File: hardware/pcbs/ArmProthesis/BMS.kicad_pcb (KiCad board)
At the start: 4 copper layers, 96.9 x 57 mm, 59 parts, among them J1 XT60-M, J2 XT60-F, J3 4-1971800-1, Q1 BSC014N04LSIATMA1, Q2 BSC014N04LSIATMA1, Q3 BSS84, SW1 CK_KMS2xxG, SW2 CK_KMS2xxG, SW3 CK_KMS2xxG, U1 BQ76920PW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

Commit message: sEMG critical  issue
Corrected inaccurate DIN 1.5mm jack footprint
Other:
- board text added: "BMS v0.3"
- board text removed: "BMS v0.2"
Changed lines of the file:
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@@
 		(layer "Edge.Cuts")
 	)
-	(gr_text "BMS v0.2"
+	(gr_text "BMS v0.3"
 		(at 189.6 126.5 0)
 		(layer "B.SilkS")

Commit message: .
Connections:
- R5 pad 1: Net-(U1-VC2) -> Net-(U1-VC5)
- U1 pad 12: Net-(U1-VC2) -> Net-(U1-VC5)
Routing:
- net Net-(U1-VC5): track 0.00 -> 4.03 mm
- net Net-(U1-VC2): track 7.32 -> 3.37 mm
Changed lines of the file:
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@@
 	(net 45 "Net-(Q1-S)")
 	(net 46 "/BMS_GND")
+	(net 47 "Net-(U1-VC5)")
 	(footprint "Capacitor_SMD:C_0603_1608Metric_Pad1.08x0.95mm_HandSolder"
 		(layer "F.Cu")
@@
 			(layers "F.Cu" "F.Mask" "F.Paste")
 			(roundrect_rratio 0.25)
-			(net 13 "Net-(U1-VC2)")
+			(net 47 "Net-(U1-VC5)")
 			(pinfunction "VC5")
 			(pintype "input")
@@
 			(layers "F.Cu" "F.Mask" "F.Paste")
 			(roundrect_rratio 0.25)
-			(net 13 "Net-(U1-VC2)")
+			(net 47 "Net-(U1-VC5)")
 			(pintype "passive")
 		)
@@
 	(gr_rect
 		(start 154.0545 94.25)
-		(end 155.4545 96.385)
+		(end 155.4545 95.738247)
 		(stroke
 			(width 0.2)
@@
 	)
 	(segment
-		(start 157.62 97.495)
-		(end 156.42 96.295)
-		(width 0.3)
-		(layer "F.Cu")
-		(net 13)
-	)
-	(segment
-		(start 154.802 95.59)
-		(end 154.747 95.645)
+		(start 156.422775 94.997775)
+		(end 156.9475 95.5225)
 		(width 0.3)
 		(layer "F.Cu")
@@
 	)
 	(segment
-		(start 157.902 95.525)
+		(start 156.9475 95.5225)
 		(end 157.9045 95.5225)
 		(width 0.3)
@@
 	)
 	(segment
-		(start 156.42 96.295)
-		(end 154.747 96.295)
-		(width 0.3)
-		(layer "F.Cu")
-		(net 13)
-	)
-	(segment
-		(start 158.28 97.495)
-		(end 157.62 97.495)
-		(width 0.3)
-		(layer "F.Cu")
-		(net 13)
-	)
-	(segment
-		(start 154.867 95.525)
-		(end 157.902 95.525)
-		(width 0.3)
-		(layer "F.Cu")
-		(net 13)
-	)
-	(segment
-		(start 154.747 95.645)
-		(end 154.867 95.525)
+		(start 154.7545 94.997775)
+		(end 156.422775 94.997775)
 		(width 0.3)
 		(layer "F.Cu")
@@
 		(net 46)
 	)
+	(segment
+		(start 157.62 97.495)
+		(end 156.42 96.295)
+		(width 0.3)
+		(layer "F.Cu")
+		(net 47)
+	)
+	(segment
+		(start 156.42 96.295)
+		(end 154.747 96.295)
+		(width 0.3)
+		(layer "F.Cu")
+		(net 47)
+	)
+	(segment
+		(start 158.28 97.495)
+		(end 157.62 97.495)
+		(width 0.3)
+		(layer "F.Cu")
+		(net 47)
+	)
 	(zone

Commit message: Corrected BMS connection
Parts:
- moved R13 0.43 mm to (130.1, 97.2)
- moved U2 0.43 mm to (129.2, 94.0)
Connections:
- R13 pad 2: Net-(U1-VC1) -> PACK+
- SW1 pad 1: Net-(U1-VC1) -> PACK+
- U2 pad 1: Net-(U1-VC1) -> PACK+
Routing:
- net Net-(U1-VC1): track 39.2 -> 3.54 mm, vias 2 -> 0
- net PACK+: track 121.0 -> 146.0 mm
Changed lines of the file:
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@@
 	(footprint "Resistor_SMD:R_0603_1608Metric_Pad0.98x0.95mm_HandSolder"
 		(layer "F.Cu")
-		(at 130.525 97.25)
+		(at 130.1 97.25)
 		(descr "Resistor SMD 0603 (1608 Metric), square (rectangular) end terminal, IPC_7351 nominal with elongated pad for handsoldering. (Body size source: IPC-SM-782 page 72, https://www.pcb-3d.com/wordpress/wp-content/uploads/ipc-sm-782a_amendment_1_and_2.pdf), generated with kicad-footprint-generator")
 		(tags "resistor handsolder")
@@
 			(layers "F.Cu" "F.Mask" "F.Paste")
 			(roundrect_rratio 0.25)
-			(net 11 "Net-(U1-VC1)")
+			(net 26 "PACK+")
 			(pintype "passive")
 		)
@@
 	(footprint "Package_TO_SOT_SMD:SOT-23-6_Handsoldering"
 		(layer "F.Cu")
-		(at 129.65 93.95 180)
+		(at 129.225 93.95 180)
 		(descr "6-pin SOT-23 package, Handsoldering")
 		(tags "SOT-23-6 Handsoldering")
@@
 			(layers "F.Cu" "F.Mask" "F.Paste")
 			(roundrect_rratio 0.25)
-			(net 11 "Net-(U1-VC1)")
+			(net 26 "PACK+")
 			(pinfunction "VCCA")
 			(pintype "power_in")
@@
 			(layers "F.Cu" "F.Mask" "F.Paste")
 			(roundrect_rratio 0.15)
-			(net 11 "Net-(U1-VC1)")
+			(net 26 "PACK+")
 			(pinfunction "1")
 			(pintype "passive")
@@
 			(layers "F.Cu" "F.Mask" "F.Paste")
 			(roundrect_rratio 0.15)
-			(net 11 "Net-(U1-VC1)")
+			(net 26 "PACK+")
 			(pinfunction "1")
 			(pintype "passive")
@@
 	)
 	(segment
-		(start 128.3 94.9)
-		(end 126.75 94.9)
+		(start 127.875 94.9)
+		(end 126.325 94.9)
 		(width 0.5)
 		(layer "F.Cu")
@@
 	)
 	(via
-		(at 126.75 94.9)
+		(at 126.325 94.9)
 		(size 0.8)
 		(drill 0.4)
@@
 	)
 	(segment
-		(start 134.5 95.2)
-		(end 133.5158 95.2)
-		(width 0.5)
-		(layer "F.Cu")
-		(net 7)
-	)
-	(segment
 		(start 162.987 92.47)
 		(end 162.977 92.48)
@@
 	)
 	(segment
+		(start 134.5 95.2)
+		(end 133.5158 95.2)
+		(width 0.5)
+		(layer "F.Cu")
+		(net 7)
+	)
+	(segment
 		(start 147.855 92.395)
 		(end 149.022 92.395)
@@
 	)
 	(segment
-		(start 131 93.95)
-		(end 132.575 93.95)
-		(width 0.5)
-		(layer "F.Cu")
-		(net 7)
-	)
-	(segment
 		(start 141.1 95.55)
 		(end 141.1045 95.5455)
@@
 	)
 	(segment
+		(start 130.7125 93.95)
+		(end 132.05 93.95)
+		(width 0.5)
+		(layer "F.Cu")
+		(net 7)
+	)
+	(segment
 		(start 151.4125 88.1)
 		(end 151.4125 89.1)
@@
 	)
 	(via
-		(at 132.575 93.95)
+		(at 132.05 93.95)
 		(size 0.8)
 		(drill 0.4)
@@
 	)
 	(segment
-		(start 131 94.9)
-		(end 131.85 94.9)
-		(width 0.3)
-		(layer "F.Cu")
-		(net 11)
-	)
-	(segment
-		(start 131.85 94.9)
-		(end 133.535 96.585)
-		(width 0.3)
-		(layer "F.Cu")
-		(net 11)
-	)
-	(segment
-		(start 135.175 93.2)
-		(end 135.175 97.2)
-		(width 0.3)
-		(layer "F.Cu")
-		(net 11)
-	)
-	(segment
-		(start 131.4375 97.25)
-		(end 133.535 97.25)
-		(width 0.3)
-		(layer "F.Cu")
-		(net 11)
-	)
-	(segment
-		(start 133.535 96.585)
-		(end 133.535 97.25)
-		(width 0.3)
-		(layer "F.Cu")
-		(net 11)
-	)
-	(segment
 		(start 157.35 93.695)
 		(end 157.355 93.7)
@@
 	)
 	(segment
-		(start 153.3095 93.695)
-		(end 153.3045 93.7)
-		(width 0.3)
-		(layer "F.Cu")
-		(net 11)
-	)
-	(segment
-		(start 133.535 97.25)
-		(end 135.125 97.25)
-		(width 0.5)
-		(layer "F.Cu")
-		(net 11)
-	)
-	(segment
-		(start 154.747 93.695)
-		(end 153.3095 93.695)
-		(width 0.3)
-		(layer "F.Cu")
-		(net 11)
-	)
-	(via
-		(at 133.535 97.25)
-		(size 0.8)
-		(drill 0.4)
-		(layers "F.Cu" "B.Cu")
-		(net 11)
-	)
-	(via
-		(at 153.3045 93.7)
-		(size 0.8)
-		(drill 0.4)
-		(layers "F.Cu" "B.Cu")
-		(net 11)
-	)
-	(segment
-		(start 138.775 92)
-		(end 133.535 97.24)
-		(width 0.3)
-		(layer "B.Cu")
-		(net 11)
-	)
-	(segment
-		(start 151.6045 92)
-		(end 138.775 92)
-		(width 0.3)
-		(layer "B.Cu")
-		(net 11)
-	)
-	(segment
-		(start 153.3045 93.7)
-		(end 151.6045 92)
-		(width 0.3)
-		(layer "B.Cu")
-		(net 11)
-	)
-	(segment
-		(start 133.535 97.24)
-		(end 133.535 97.25)
-		(width 0.3)
-		(layer "B.Cu")
-		(net 11)
-	)
-	(segment
 		(start 156.355 93.045)
 		(end 157.625 91.775)
@@
 	)
 	(segment
+		(start 135.125 97.25)
+		(end 131.4375 97.25)
+		(width 0.5)
+		(layer "F.Cu")
+		(net 26)
+	)
+	(segment
+		(start 135.175 104.025)
+		(end 133.5 105.7)
+		(width 0.3)
+		(layer "F.Cu")
+		(net 26)
+	)
+	(segment
+		(start 135.3 97.075)
+		(end 135.3 93.325)
+		(width 0.5)
+		(layer "F.Cu")
+		(net 26)
+	)
+	(segment
 		(start 120.425 96.875)
 		(end 129.25 105.7)
@@
 	)
 	(segment
+		(start 131.8 94.9)
+		(end 130.575 94.9)
+		(width 0.5)
+		(layer "F.Cu")
+		(net 26)
+	)
+	(segment
+		(start 135.125 97.25)
+		(end 134.15 97.25)
+		(width 0.5)
+		(layer "F.Cu")
+		(net 26)
+	)
+	(segment
 		(start 129.25 105.7)
-		(end 172.375 105.7)
+		(end 133.5 105.7)
 		(width 3.7)
 		(layer "F.Cu")
@@
 	)
 	(segment
+		(start 135.125 104.075)
+		(end 133.5 105.7)
+		(width 0.5)
+		(layer "F.Cu")
+		(net 26)
+	)
+	(segment
 		(start 107.3 107.7)
 		(end 110.3 107.7)
@@
 	)
 	(segment
+		(start 134.15 97.25)
+		(end 131.8 94.9)
+		(width 0.5)
+		(layer "F.Cu")
+		(net 26)
+	)
+	(segment
 		(start 172.375 105.7)
 		(end 181.3 96.775)
@@
 		(net 26)
 	)
+	(segment
+		(start 135.3 93.325)
+		(end 135.125 93.15)
+		(width 0.5)
+		(layer "F.Cu")
+		(net 26)
+	)
+	(segment
+		(start 135.125 97.25)
+		(end 135.125 104.075)
+		(width 0.5)
+		(layer "F.Cu")
+		(net 26)
+	)
+	(segment
+		(start 135.125 97.25)
+		(end 135.3 97.075)
+		(width 0.5)
+		(layer "F.Cu")
+		(net 26)
+	)
+	(segment
+		(start 133.5 105.7)
+		(end 172.375 105.7)
+		(width 3.7)
+		(layer "F.Cu")
+		(net 26)
+	)
 	(via
 		(at 107.3 107.7)
@@
 	)
 	(segment
-		(start 129.625 94.3)
-		(end 129.625 97.2375)
+		(start 129.2 94.3)
+		(end 129.2 97.2375)
 		(width 0.3)
 		(layer "F.Cu")
@@
 	)
 	(segment
-		(start 129.275 93.95)
-		(end 129.625 94.3)
+		(start 128.85 93.95)
+		(end 129.2 94.3)
 		(width 0.3)
 		(layer "F.Cu")
@@
 	)
 	(segment
-		(start 128.3 93.95)
-		(end 129.275 93.95)
+		(start 127.875 93.95)
+		(end 128.85 93.95)
 		(width 0.3)
 		(layer "F.Cu")
@@
 	)
 	(segment
-		(start 126.75 93)
-		(end 128.3 93)
+		(start 126.325 93)
+		(end 127.875 93)
 		(width 0.5)
 		(layer "F.Cu")
@@
 	)
 	(via
-		(at 126.75 93)
+		(at 126.325 93)
 		(size 0.8)
 		(drill 0.4)

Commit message: BMS v0.5 still not resized
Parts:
- removed R13: 10k, Resistor_SMD:R_0603_1608Metric_Pad0.98x0.95mm_HandSolder
- removed U2: SN74LVC1T45DCK, Package_TO_SOT_SMD:SOT-23-6_Handsoldering
- added SW4: CK_KMS2xxG, Button_Switch_SMD:SW_SPST_CK_KMS2xxG, F.Cu at (168.1, 117.7)
- R12: value 47k -> 1k; footprint Resistor_SMD:R_0603_1608Metric_Pad0.98x0.95mm_HandSolder -> Resistor_SMD:R_0402_1005Metric_Pad0.72x0.64mm_HandSolder
- moved R12 40.4 mm to (163.8, 118.5), turned to 0 degrees
- moved REF** 2.16 mm to (179.3, 121.0)
- moved R8 2.14 mm to (150.3, 102.0), turned to 0 degrees
- moved R19 0.98 mm to (158.1, 115.8), turned to 90 degrees
- moved C11 0.34 mm to (150.5, 99.6)
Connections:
- R12 pad 1: Net-(D1-A) -> PWROFF
- R12 pad 2: PACK- -> Net-(R12-Pad2)
- SW1 pad 1: PACK+ -> Net-(U1-VC1)
- U5 pad 3: PA12 -> PA11
- U5 pad 4: PA11 -> PA12
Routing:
- net PACK+: track 146.0 -> 6.90 mm, vias 4 -> 5
- net /BMS_GND: track 70.1 -> 13.6 mm, vias 4 -> 14
- net PWROFF: track 40.8 -> 9.52 mm
- net Net-(U1-VC1): track 3.54 -> 31.5 mm, vias 0 -> 2
- net +3.3V: track 75.4 -> 57.2 mm, vias 5 -> 4
- net Net-(D1-A): track 14.8 -> 6.93 mm
- net Net-(R12-Pad2): track 0.00 -> 5.82 mm
- net Net-(U2-DIR): track 4.41 -> 0.00 mm
- net PA11: track 14.6 -> 11.3 mm
- net PA12: track 13.3 -> 15.7 mm
- net PACK-: track 30.2 -> 28.4 mm, vias 25 -> 34
- added copper zone on In1.Cu, net /BMS_GND
- added copper zone on In2.Cu, net /BMS_GND
- added copper zone on In2.Cu, net PACK+
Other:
- board text added: "BMS v0.5"
- board text removed: "BMS v0.3"

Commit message: .
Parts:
- removed G***: LOGO, Pics:riven_sword_20mm_quality
- removed REF**: riven_sword_20mm_quality_mirrored, Pics:riven_sword_20mm_quality_mirrored
- moved H1 18.6 mm to (126.5, 78.5)
- moved H3 18.6 mm to (126.5, 125.7)
- moved U3 18.1 mm to (125.0, 107.0)
- moved U4 18.1 mm to (125.0, 114.5)
- moved H2 14.0 mm to (181.0, 78.6)
- moved H4 14.0 mm to (181.0, 125.8)
- moved J3 14.0 mm to (175.6, 114.5)
- moved J1 12.4 mm to (168.9, 89.3)
- moved J2 9.31 mm to (129.7, 88.9)
- moved SW1 0.48 mm to (136.4, 95.2)
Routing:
- net Net-(C9-Pad1): track 38.4 -> 25.1 mm
- net Net-(C8-Pad1): track 39.0 -> 26.4 mm
- net Net-(C7-Pad1): track 38.4 -> 26.6 mm
- net Net-(C6-Pad2): track 39.7 -> 30.9 mm
- net Net-(U1-VC1): track 31.5 -> 34.6 mm
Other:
- board size 96.9 x 57 mm -> 64.1 x 55.2 mm

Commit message: updates
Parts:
- removed C15: 0.1uF, Capacitor_SMD:C_0402_1005Metric_Pad0.74x0.62mm_HandSolder
- removed R14: 330, Resistor_SMD:R_0402_1005Metric_Pad0.72x0.64mm_HandSolder
- removed R15: 10k, Resistor_SMD:R_0402_1005Metric_Pad0.72x0.64mm_HandSolder
- removed SW3: CK_KMS2xxG, Button_Switch_SMD:SW_SPST_CK_KMS2xxG
- C1, C13, C14, C2, C3, C4, C5: footprint Capacitor_SMD:C_0603_1608Metric_Pad1.08x0.95mm_HandSolder -> Capacitor_SMD:C_0603_1608Metric
- C10, C12: footprint Capacitor_SMD:C_0402_1005Metric_Pad0.74x0.62mm_HandSolder -> Capacitor_SMD:C_0402_1005Metric
- C11: footprint Capacitor_SMD:C_1210_3225Metric_Pad1.33x2.70mm_HandSolder -> Capacitor_SMD:C_1210_3225Metric
- C6, C7, C8, C9: footprint Capacitor_SMD:C_0805_2012Metric_Pad1.18x1.45mm_HandSolder -> Capacitor_SMD:C_0603_1608Metric
- D2: footprint Diode_SMD:D_0603_1608Metric_Pad1.05x0.95mm_HandSolder -> Diode_SMD:D_0603_1608Metric
- R1: value R -> 5m; footprint Resistor:R_3920 -> Resistor_SMD:R_2512_6332Metric
- R10, R9: footprint Resistor_SMD:R_0603_1608Metric_Pad0.98x0.95mm_HandSolder -> Resistor_SMD:R_0603_1608Metric
- R11, R17, R18, R19: footprint Resistor_SMD:R_0603_1608Metric_Pad0.98x0.95mm_HandSolder -> Resistor_SMD:R_0402_1005Metric
- R12, R16, R2, R3, R4, R5, R6, R7, R8: footprint Resistor_SMD:R_0402_1005Metric_Pad0.72x0.64mm_HandSolder -> Resistor_SMD:R_0402_1005Metric
- moved SW4 2.45 mm to (165.7, 117.7)
- moved R12 2.10 mm to (162.7, 120.3)
- moved R19 1.42 mm to (159.4, 115.4), turned to 180 degrees
- moved R8 0.40 mm to (149.9, 102.0)
- moved R16 0.11 mm to (160.9, 118.9)
- moved R9 0.11 mm to (140.2, 78.3)
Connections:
- net PA13 renamed SWDIO
- net PA14 renamed SWCLK
- R12 pad 2: Net-(R12-Pad2) -> PACK-
- R5 pad 1: Net-(U1-VC5) -> Net-(U1-REGSRC)
- SW4 pad 1: Net-(R12-Pad2) -> PWROFF
- U1 pad 12: Net-(U1-VC5) -> Net-(U1-REGSRC)
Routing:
- net Net-(Q2-D): track 15.0 -> 4.84 mm
- net Net-(U1-REGSRC): track 3.53 -> 13.3 mm
- net SWCLK: track 23.3 -> 13.7 mm
- net Net-(R14-Pad2): track 7.61 -> 0.00 mm
- net PWROFF: track 9.52 -> 15.8 mm
- net Net-(R12-Pad2): track 5.82 -> 0.00 mm
- net Net-(U1-VC5): track 4.03 -> 0.00 mm
- net /BMS_GND: track 13.6 -> 17.3 mm
- net +3.3V: track 57.2 -> 53.9 mm
- net Net-(Q1-G): track 19.8 -> 17.3 mm
- net Net-(Q2-G): track 5.79 -> 4.10 mm
- net Net-(C6-Pad2): track 30.9 -> 30.2 mm
- net Net-(C7-Pad1): track 26.6 -> 27.2 mm
- net ALERT: track 32.3 -> 32.8 mm
- net PACK-: track 28.5 -> 29.0 mm, vias 34 -> 31
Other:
- board text added: "BMS v0.6"
- board text removed: "BMS v0.5"

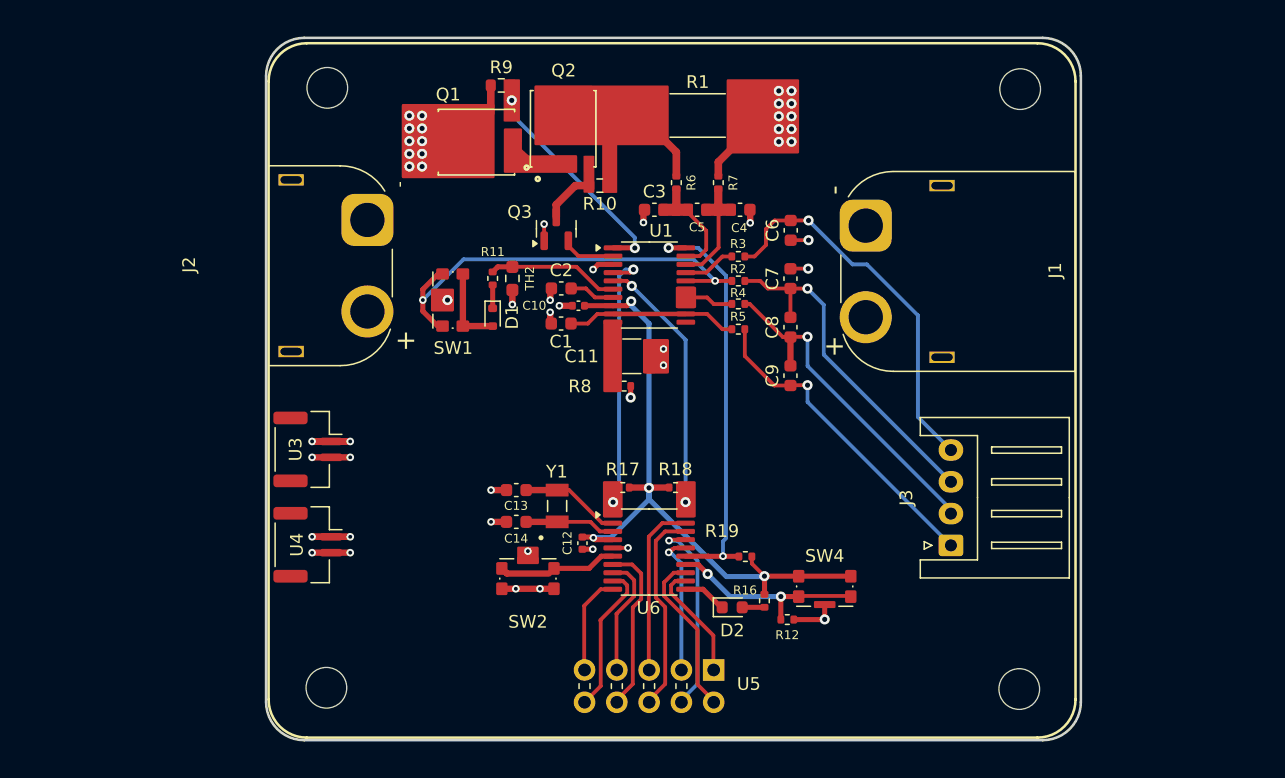
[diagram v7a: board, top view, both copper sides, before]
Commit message: bms V0.7 with BQ76905
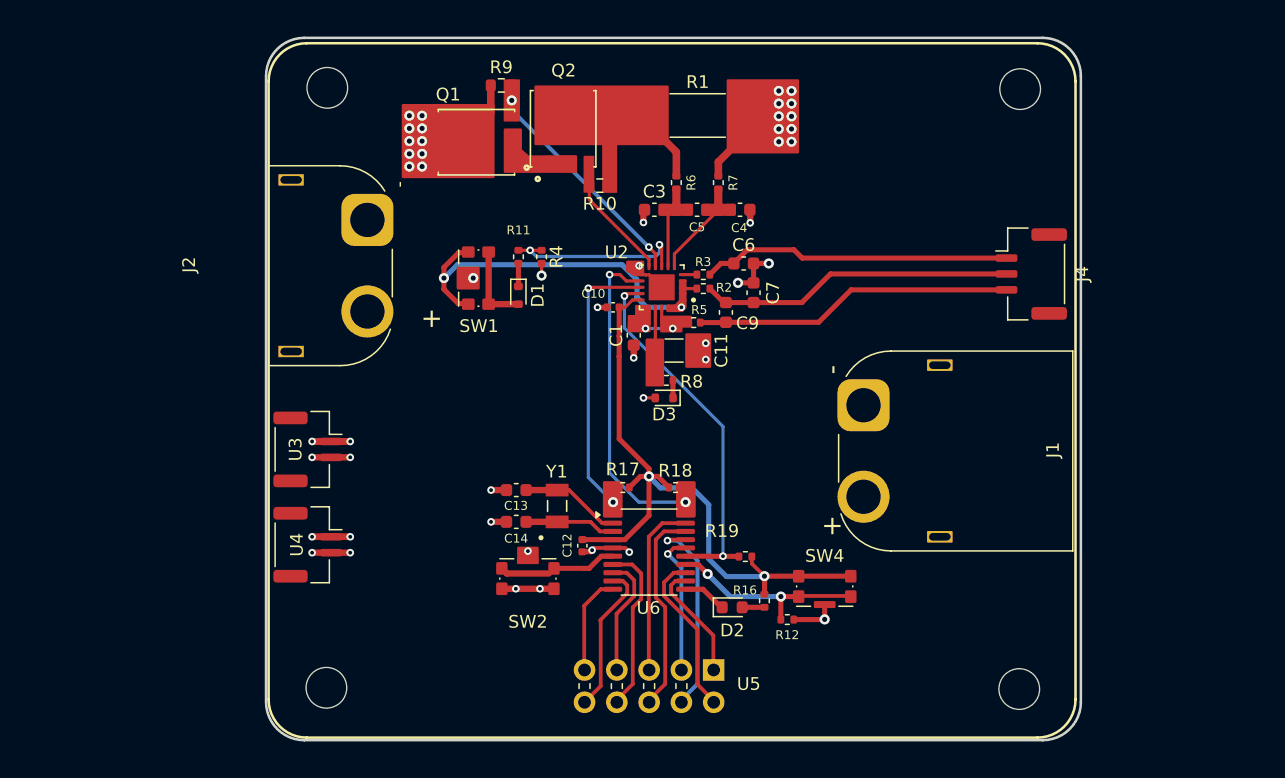
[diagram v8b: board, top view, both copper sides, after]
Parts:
- removed C2, C8: 1uF, Capacitor_SMD:C_0603_1608Metric
- removed J3: 4-1971800-1, Connector_JST:JST_XH_S4B-XH-A_1x04_P2.50mm_Horizontal
- removed Q3: BSS84, Package_TO_SOT_SMD:SOT-23
- removed TH2: Thermistor_NTC, Resistor_SMD:R_0603_1608Metric_Pad0.98x0.95mm_HandSolder
- removed U1: BQ76920PW, Package_SO:TSSOP-20_4.4x6.5mm_P0.65mm
- added D3: 1N4148WT, Diode_SMD:D_SOD-523, F.Cu at (153.0, 102.9)
- added J4: Conn_01x03, Connector_JST:JST_GH_BM03B-GHS-TBT_1x03-1MP_P1.25mm_Vertical, F.Cu at (181.9, 93.2)
- added U2: BQ76905RGRR, BMS:BQ76905RGRR, F.Cu at (152.8, 94.2)
- C11: footprint Capacitor_SMD:C_1210_3225Metric -> Capacitor_SMD:C_1206_3216Metric
- R11: value 10k -> 120k
- R4: value 100 -> 100k
- moved R4 15.9 mm to (143.4, 91.8), turned to -90 degrees
- moved J1 14.1 mm to (168.7, 103.5)
- moved C9 7.11 mm to (157.9, 96.2)
- moved C1 5.79 mm to (150.7, 98.0), turned to 90 degrees
- moved C6 4.52 mm to (159.3, 92.3), turned to 180 degrees
- moved R5 3.54 mm to (155.4, 97.0)
- moved C11 3.36 mm to (153.8, 99.2)
- moved R8 3.36 mm to (153.2, 101.5)
- moved C7 3.11 mm to (160.1, 94.6)
- moved R3 3.10 mm to (156.1, 93.2)
- moved R2 2.82 mm to (156.1, 94.3)
- moved C10 2.73 mm to (149.0, 95.8)
- moved SW1 2.66 mm to (138.4, 93.5)
- moved D1 2.66 mm to (141.6, 94.8)
- moved R11 2.64 mm to (141.6, 91.8)
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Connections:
- C7 pad 1: Net-(C7-Pad1) -> Net-(J4-Pin_2)
- C9 pad 2: Net-(C8-Pad1) -> Net-(J4-Pin_2)
- R11 pad 1: Net-(U1-TS1) -> Net-(U2-TS)
- R2 pad 2: Net-(C7-Pad1) -> Net-(J4-Pin_2)
- R4 pad 1: Net-(U1-VC2) -> Net-(U2-TS)
- R4 pad 2: Net-(C8-Pad1) -> PACK-
- R8 pad 2: PACK+ -> Net-(D3-K)
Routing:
- net Net-(C7-Pad1): track 27.2 -> 0.00 mm, vias 1 -> 0
- net Net-(C8-Pad1): track 26.4 -> 0.00 mm, vias 1 -> 0
- net Net-(J4-Pin_2): track 0.00 -> 24.7 mm
- net Net-(U2-TS): track 0.00 -> 14.7 mm, vias 0 -> 2
- net Net-(U1-TS1): track 10.4 -> 0.00 mm
- net Net-(J4-Pin_1): track 30.2 -> 24.4 mm, vias 1 -> 0
- net Net-(U2-REGSRC): track 13.3 -> 7.69 mm, vias 0 -> 2
- net Net-(U2-VC1): track 34.6 -> 29.2 mm
- net SCL: track 20.4 -> 25.6 mm
- net Net-(Q2-G): track 4.10 -> 8.29 mm
- net Net-(Q3-S): track 3.85 -> 0.00 mm
- net Net-(U1-VC2): track 3.84 -> 0.00 mm
- net ALERT: track 32.8 -> 29.2 mm
- net Net-(U1-CAP1): track 3.50 -> 0.00 mm
- net Net-(U2-BAT): track 0.00 -> 3.33 mm
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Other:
- board text added: "BMS v0.7"
- board text removed: "BMS v0.6"
